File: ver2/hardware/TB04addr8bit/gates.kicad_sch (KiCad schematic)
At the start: 16 parts, among them U1501 74AHC04, U1502 74AHC04, U1503 74LS08, U1504 74HC00, U1505 74LS00, U1506 74LS32, U1507 74LS08, U1508 74HC00

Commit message: ver2: 掃除とタイミング是正(ROMのEXEゲート・フラグクロックをFCH1へ)
- 消費先ゼロだったU1302(RAM_SEL/STACK_SEL/IN_SEL/P6)を削除し空きゲート入力をGNDへ
- /OE_ROMの条件を生の~WRから~WR_EXE(=!(WR&EXE))へ変更
  書込命令の次のフェッチでROMが閉じる問題を解消
- フラグDFFのクロックゲートをEXEからFCH1へ(CLK_C=FCH1&C_WE)
  INのZが間に合わない件と、Cin=C_prevの帰還でADD/SUBの結果が壊れる件を解消
- いずれもネットリストで接続変化を照合済み。ERCはエラー98(全てwire_dangling)・警告0

Co-Authored-By: Claude Opus 5 <noreply@anthropic.com>
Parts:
- removed unit 4 of U1502
- added unit 4 of U1501
- renumbered U1502 to U1501, U1501 to U1502
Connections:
- net P4 is gone; now on net GND: U1501.3
- net EXE: no longer U1503.1, U1503.4
- net FCH1: now also U1503.1, U1503.4
- net WR_EXE: now also U1501.9
- net ~{WR}: no longer U1504.13
- net ~{P4}: no longer names the net of U1501.4
- new net ~{WR_EXE}: U1501.8, U1504.13
- no-connect marks 5 -> 6
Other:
- moved on the sheet: U1501B, U1501E, U1501F, U1502D, U1506D

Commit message: ver2: Yドライバ/PCドライバを1チップ1機能に整理
- ram: 74HC244×2を組み替え。U1102=Yドライバ専用(YD0-3→MD0-3、
  bank2はGND→MD4-7で上位0埋め、OE2本とも~YEN_Y)、U1103=PCドライバ
  専用(PC_Q0-7→MD0-7、OE2本とも~YEN_PC)。接続の集合は変更前と完全
  一致で機能等価。PCの8bitが1チップに揃いビット間スキューが揃う
- inPut: U1001のbank2イネーブル(pin19)をVDDから~OE_iAddrへ。
  出力2Y0-3はno_connectのままなので効果は未発現
- addrMUX/sp: 未使用出力のスタブ位置調整のみ(接続変更なし)

Co-Authored-By: Claude Opus 5 <noreply@anthropic.com>
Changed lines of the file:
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@@
 	)
 	(global_label "WR"
-		(shape input)
+		(shape output)
 		(at 55.88 35.56 0)
 		(fields_autoplaced yes)

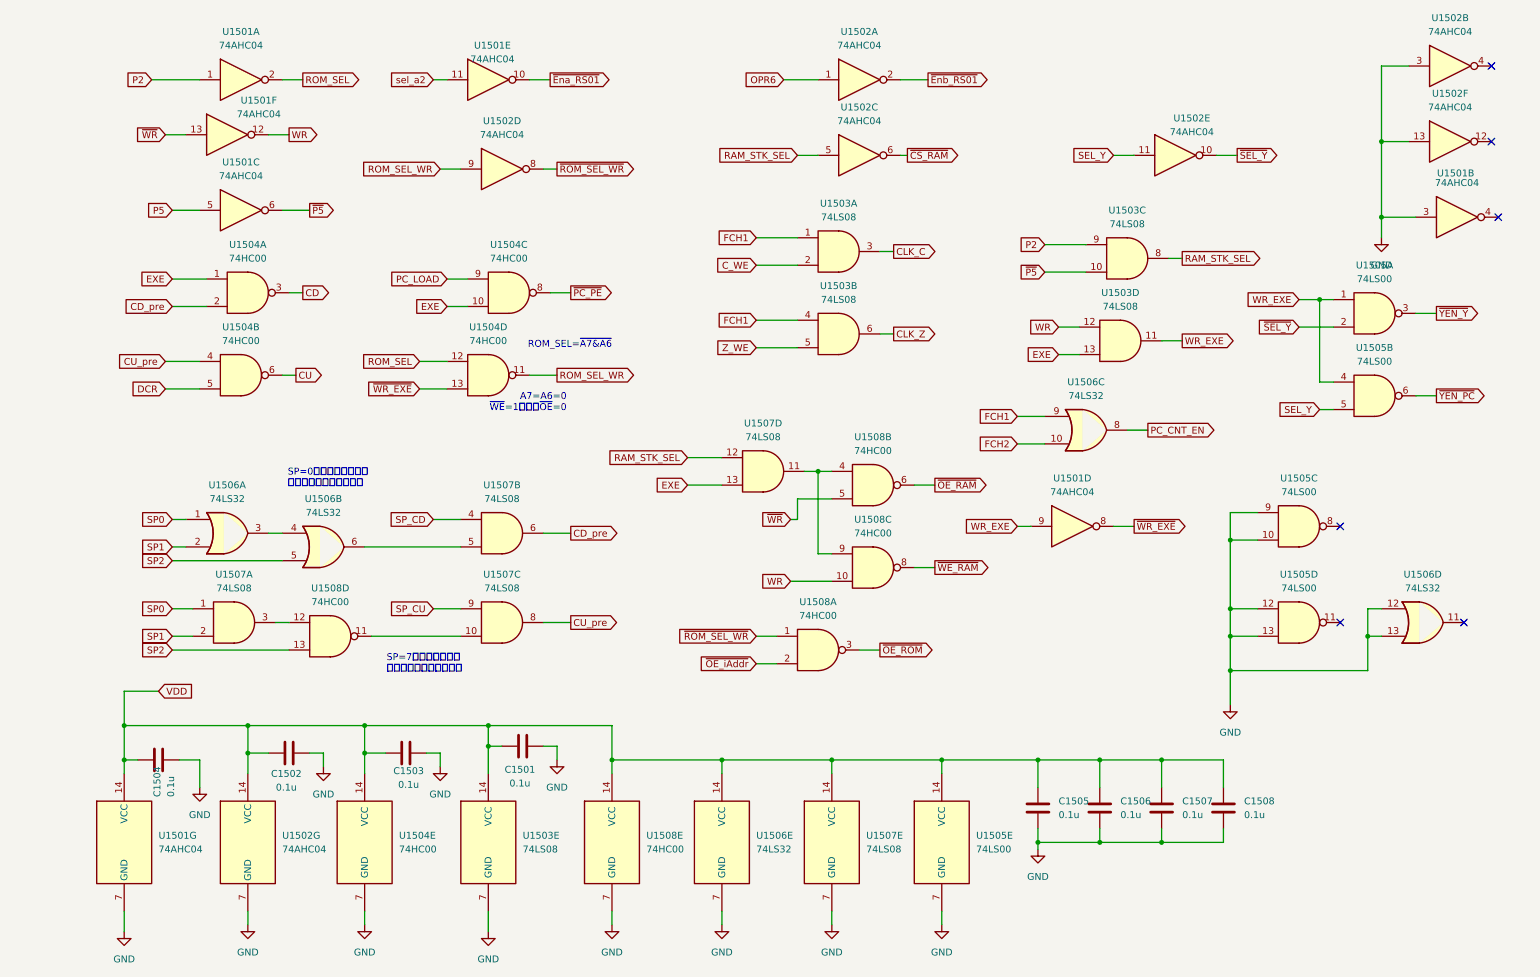
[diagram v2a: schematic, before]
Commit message: ver2: CALLの書込タイミングを是正(RAM書込パルスをCLK_CPUでゲート)
~WE_RAM = !(RAM_STK_SEL & EXE & WR & CLK_CPU) に変更し、
EXE前半のCLK立下りで書込を確定させる。CALLが戻り番地でなく
分岐先をスタックに書く問題を解消。gatesシートの空きゲート
(U1502インバータ・U1505 NAND g3)を使い追加ICは0個。

Co-Authored-By: Claude Opus 5 <noreply@anthropic.com>
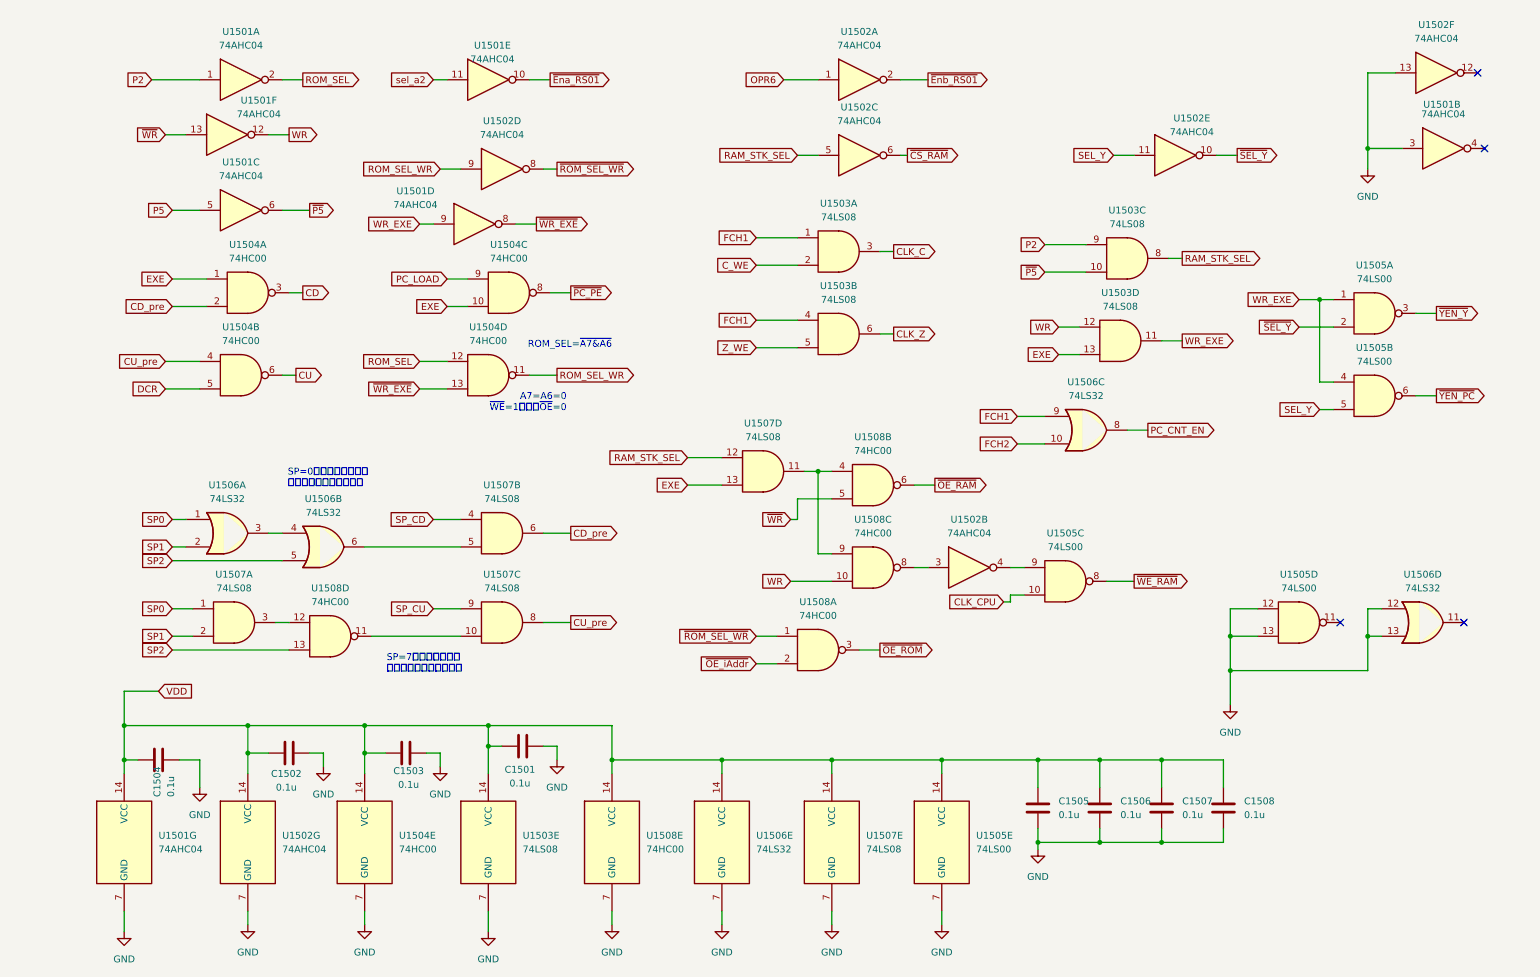
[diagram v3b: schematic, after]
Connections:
- net GND: no longer U1502.3, U1505.10, U1505.9
- net ~{WE_RAM}: now also U1505.8; no longer U1508.8
- net at U1502.4: now also U1505.9
- new net: U1502.3, U1508.8
- new net CLK_CPU: U1505.10
- no-connect marks 6 -> 4
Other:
- moved on the sheet: U1501B, U1501D, U1502B, U1502F, U1505C

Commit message: ver2: I/Oを4ch化しアドレスバスの浮きを解消(OUTは377化・RAMのCSをEXEゲート)
- I/Oアドレス源244・port位置MUX157・portデコード139を追加し、IN244×4/OUT×4に拡張。
  IN/OUT実行中も 0xF8|port / 0xFC|port をアドレスバスへ出すことで、全相・全命令で
  アドレスバスが必ず1つに駆動される状態にした(OUTのRAM誤書込・INのMD衝突を構造的に解消)。
- OUTポートを74HC273→74HC377へ。~E=139出力・CP=~CLK_CPUとし、クロックゲートなしで
  EXE中間の1回だけ取り込む(取り込み余裕が15ns→半相)。
- ~CS_RAM を !(RAM_STK_SEL & EXE) に変更(CS_RAMノード新設)。EXE末に出る第2の書込パルスを
  約38nsに短縮しtWP未満に収めた。フェッチ3相でRAMが非選択になる副次効果あり。
- OUTコネクタのピン配列を7segIF J1に合わせて入れ替え(D3出力がVDDへ短絡する組合せを回避)。
- パスコンが無かった2シート(outPort・PC_aluMux)に追加。RS.kicad_sch を RS00.kicad_sch へ改名。

Co-Authored-By: Claude Opus 5 <noreply@anthropic.com>
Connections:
- net EXE: now also U1505.13
- net GND: no longer U1505.12, U1505.13
- net RAM_STK_SEL: no longer U1502.5
- net CS_RAM: now reaches U1507.11, U1508.4, U1508.9
- net CS_RAM: now also U1502.5
- net ~{OE_ioAddr}: now reaches U1505.11
- new net SEL_M1: U1505.12
- no-connect marks 4 -> 3
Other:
- moved on the sheet: U1505D, U1506D

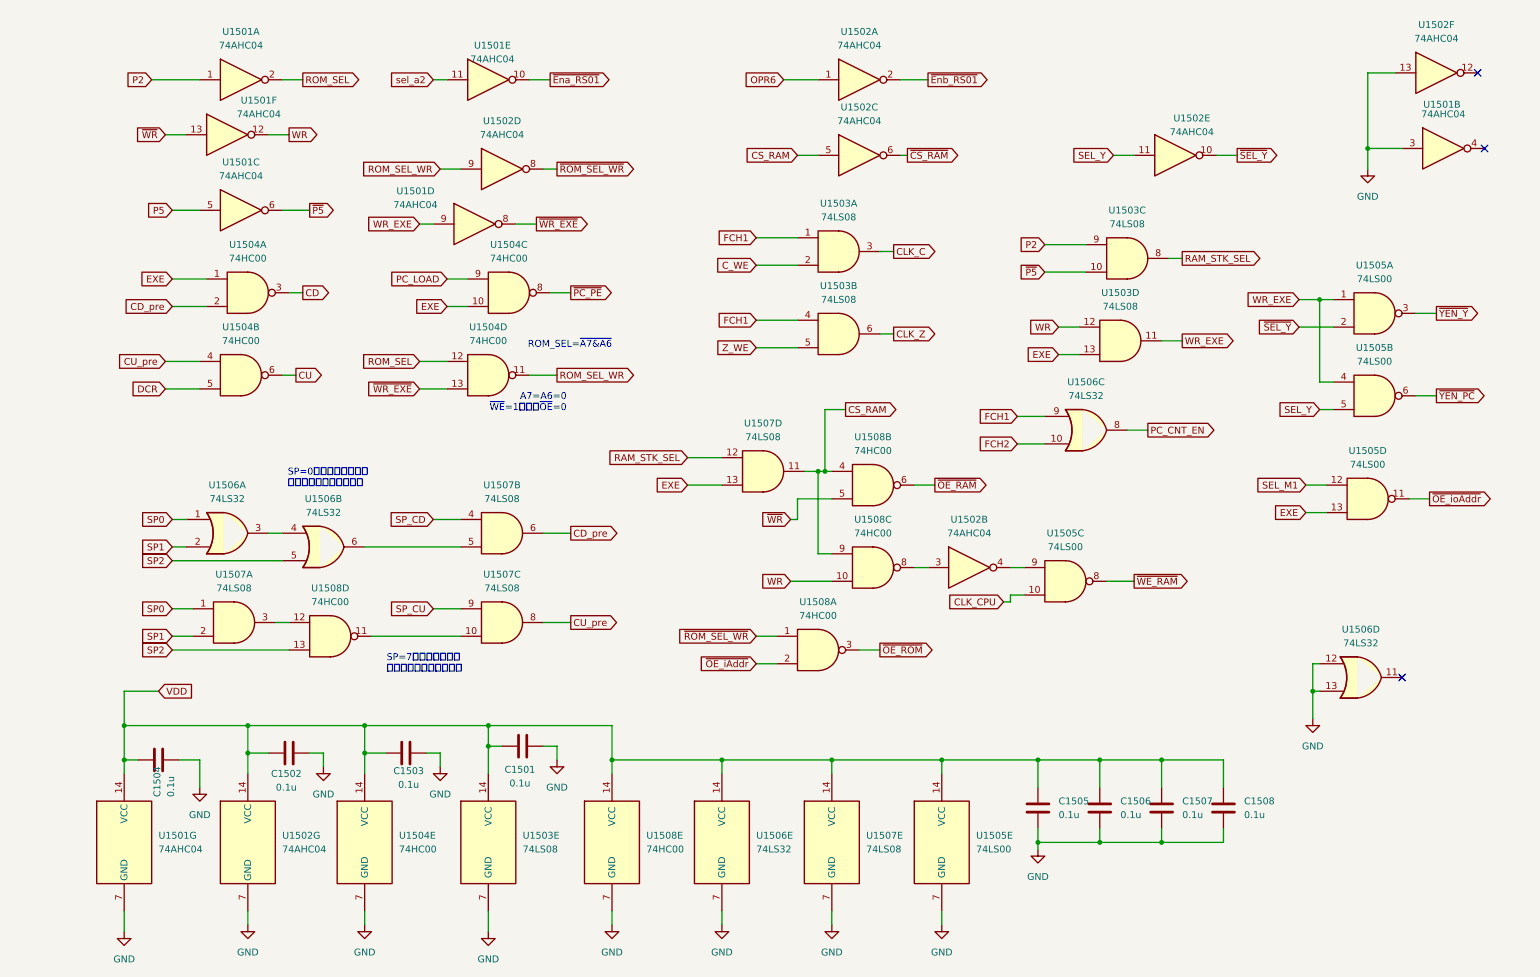
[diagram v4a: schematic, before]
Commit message: ver2: SPアップカウントのヒゲを除去(CUをCLK_CPUでマスク)
CU=!(CU_pre & DCR)のCU_preがDCR自身でクロックされる制御ラッチU701から
来ているため、POP/RETの次の命令のDCR立上りで幅22-46nsのヒゲが出てSPが
余分に+1されていた(3段以上のネストで戻り番地がずれる)。

U1506の空きORゲートでCU=!(CU_pre & DCR & ~CLK_CPU)とし、DCR開始時は
CLK_CPUがHなのでヒゲをマスクする。カウント用の立上りは従来どおり
DCR→EXEの境目に出るのでプリインクリメントの意味は変わらない。

Co-Authored-By: Claude Opus 5 <noreply@anthropic.com>
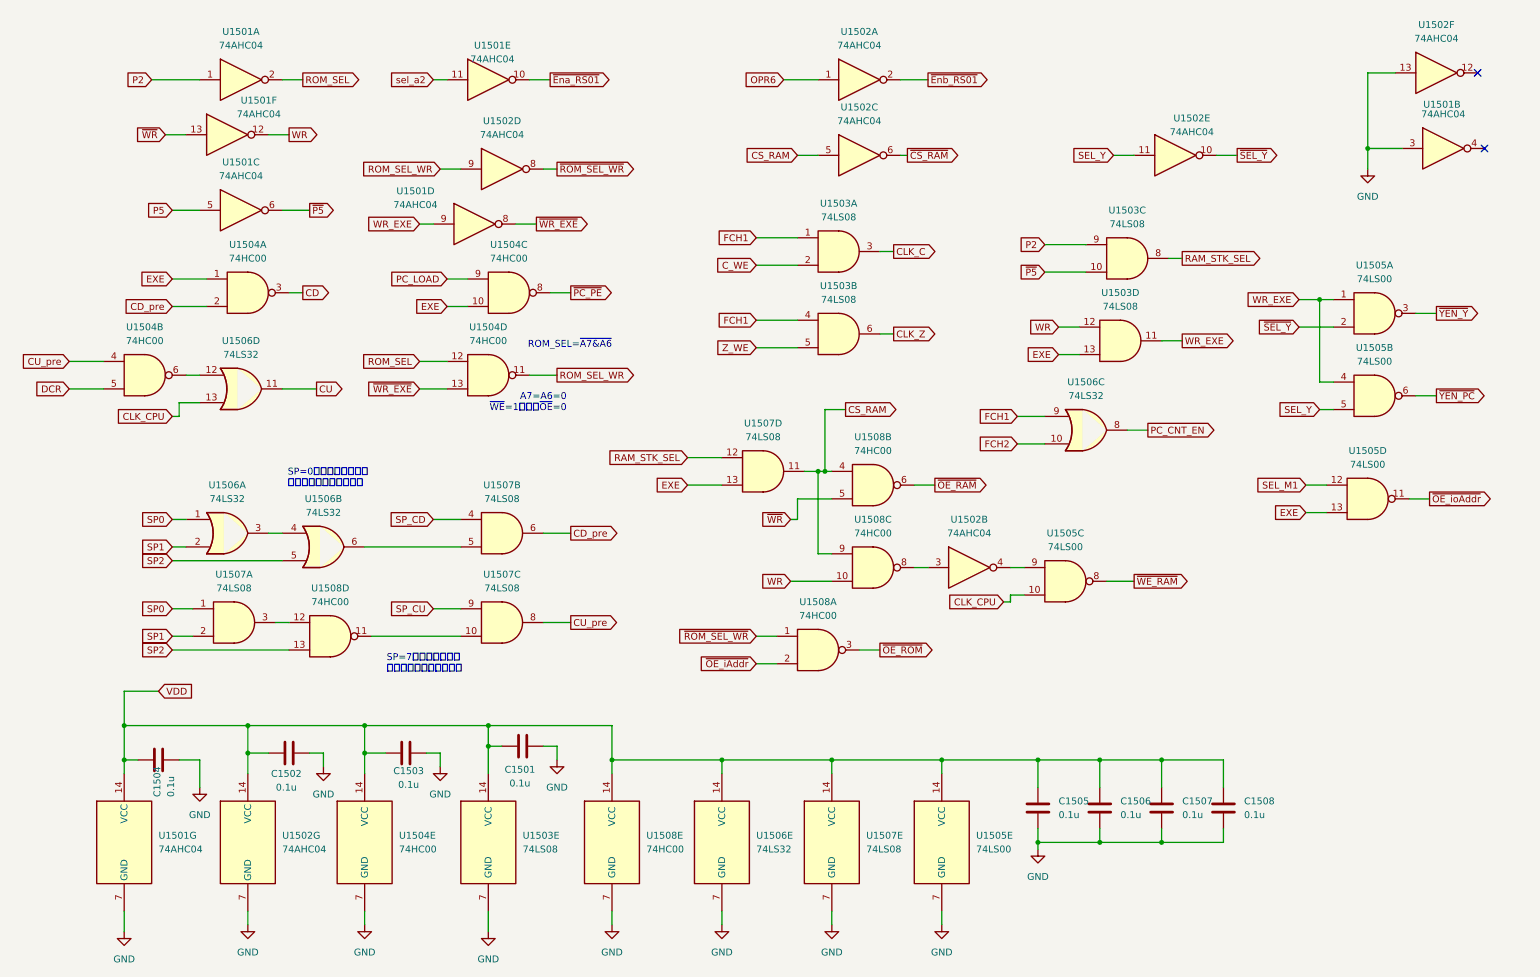
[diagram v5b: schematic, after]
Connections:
- net CLK_CPU: now also U1506.13
- net CU: now also U1506.11; no longer U1504.6
- net GND: no longer U1506.12, U1506.13
- new net: U1504.6, U1506.12
- no-connect marks 3 -> 2
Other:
- moved on the sheet: U1504B, U1506D
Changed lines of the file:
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@@
 	)
 	(junction
-		(at 245.11 138.43)
-		(diameter 0)
-		(color 0 0 0 0)
-	)
-	(junction
 		(at 154.94 97.79)
 		(diameter 0)
@@
 	)
 	(no_connect
-		(at 261.62 135.89)
-	)
-	(no_connect
 		(at 276.86 38.1)
 	)
@@
 	(wire
 		(pts
-			(xy 245.11 138.43) (xy 246.38 138.43)
-		)
-		(stroke
-			(width 0)
-			(type default)
-		)
-	)
-	(wire
-		(pts
 			(xy 217.17 151.13) (xy 217.17 156.21)
 		)
@@
 	(wire
 		(pts
+			(xy 35.56 87.63) (xy 35.56 85.09)
+		)
+		(stroke
+			(width 0)
+			(type default)
+		)
+	)
+	(wire
+		(pts
 			(xy 255.27 38.1) (xy 261.62 38.1)
 		)
@@
 	(wire
 		(pts
+			(xy 34.29 87.63) (xy 35.56 87.63)
+		)
+		(stroke
+			(width 0)
+			(type default)
+		)
+	)
+	(wire
+		(pts
 			(xy 48.26 149.86) (xy 52.07 149.86)
 		)
@@
 	(wire
 		(pts
-			(xy 33.02 77.47) (xy 39.37 77.47)
+			(xy 15.24 77.47) (xy 21.59 77.47)
 		)
 		(stroke
@@
 	(wire
 		(pts
-			(xy 33.02 82.55) (xy 39.37 82.55)
+			(xy 15.24 82.55) (xy 21.59 82.55)
 		)
 		(stroke
@@
 	(wire
 		(pts
-			(xy 245.11 133.35) (xy 245.11 138.43)
-		)
-		(stroke
-			(width 0)
-			(type default)
-		)
-	)
-	(wire
-		(pts
 			(xy 195.58 60.96) (xy 203.2 60.96)
 		)
@@
 	(wire
 		(pts
-			(xy 54.61 25.4) (xy 58.42 25.4)
+			(xy 54.61 82.55) (xy 60.96 82.55)
 		)
 		(stroke
@@
 	(wire
 		(pts
-			(xy 153.67 97.79) (xy 154.94 97.79)
+			(xy 54.61 25.4) (xy 58.42 25.4)
 		)
 		(stroke
@@
 	(wire
 		(pts
-			(xy 30.48 25.4) (xy 39.37 25.4)
+			(xy 153.67 97.79) (xy 154.94 97.79)
 		)
 		(stroke
@@
 	(wire
 		(pts
-			(xy 135.89 151.13) (xy 156.21 151.13)
+			(xy 30.48 25.4) (xy 39.37 25.4)
 		)
 		(stroke
@@
 	(wire
 		(pts
-			(xy 135.89 151.13) (xy 135.89 153.67)
+			(xy 135.89 151.13) (xy 156.21 151.13)
 		)
 		(stroke
@@
 	(wire
 		(pts
-			(xy 246.38 133.35) (xy 245.11 133.35)
+			(xy 135.89 151.13) (xy 135.89 153.67)
 		)
 		(stroke
@@
 	(wire
 		(pts
-			(xy 54.61 80.01) (xy 57.15 80.01)
+			(xy 36.83 80.01) (xy 39.37 80.01)
 		)
 		(stroke
@@
 	(wire
 		(pts
-			(xy 245.11 138.43) (xy 245.11 143.51)
-		)
-		(stroke
-			(width 0)
-			(type default)
-		)
-	)
-	(wire
-		(pts
 			(xy 264.16 83.82) (xy 267.97 83.82)
 		)
@@
 		)
 	)
+	(wire
+		(pts
+			(xy 35.56 85.09) (xy 39.37 85.09)
+		)
+		(stroke
+			(width 0)
+			(type default)
+		)
+	)
 	(global_label "FCH1"
 		(shape input)
@@
 		)
 	)
+	(global_label "CLK_CPU"
+		(shape input)
+		(at 34.29 87.63 180)
+		(fields_autoplaced yes)
+		(effects
+			(font
+				(size 1.27 1.27)
+			)
+			(justify right)
+		)
+		(property "Intersheetrefs" "${INTERSHEET_REFS}"
+			(at 22.8986 87.63 0)
+			(show_name no)
+			(do_not_autoplace no)
+			(effects
+				(font
+					(size 1.27 1.27)
+				)
+				(justify right)
+			)
+		)
+	)
 	(global_label "P2"
 		(shape input)
@@
 	(global_label "DCR"
 		(shape input)
-		(at 33.02 82.55 180)
+		(at 15.24 82.55 180)
 		(fields_autoplaced yes)
 		(effects
@@
 		)
 		(property "Intersheetrefs" "${INTERSHEET_REFS}"
-			(at 23.5034 82.55 0)
+			(at 5.7234 82.55 0)
 			(show_name no)
 			(do_not_autoplace no)
@@
 	(global_label "CU"
 		(shape output)
-		(at 57.15 80.01 0)
+		(at 60.96 82.55 0)
 		(fields_autoplaced yes)
 		(effects
@@
 		)
 		(property "Intersheetrefs" "${INTERSHEET_REFS}"
-			(at 62.7357 80.01 0)
+			(at 66.5457 82.55 0)
 			(show_name no)
 			(do_not_autoplace no)
@@
 	(global_label "CU_pre"
 		(shape input)
-		(at 33.02 77.47 180)
+		(at 15.24 77.47 180)
 		(fields_autoplaced yes)
 		(effects
@@
 		)
 		(property "Intersheetrefs" "${INTERSHEET_REFS}"
-			(at 23.4429 77.47 0)
+			(at 5.6629 77.47 0)
 			(show_name no)
 			(do_not_autoplace no)
@@
 	)
 	(symbol
-		(lib_id "power:GND")
-		(at 245.11 143.51 0)
-		(unit 1)
-		(body_style 1)
-		(exclude_from_sim no)
-		(in_bom yes)
-		(on_board yes)
-		(in_pos_files yes)
-		(dnp no)
-		(fields_autoplaced yes)
-		(property "Reference" "#PWR01502"
-			(at 245.11 149.86 0)
-			(hide yes)
-			(show_name no)
-			(do_not_autoplace no)
-			(effects
-				(font
-					(size 1.27 1.27)
-				)
-			)
-		)
-		(property "Value" "GND"
-			(at 245.11 148.59 0)
-			(show_name no)
-			(do_not_autoplace no)
-			(effects
-				(font
-					(size 1.27 1.27)
-				)
-			)
-		)
-		(property "Footprint" ""
-			(at 245.11 143.51 0)
-			(hide yes)
-			(show_name no)
-			(do_not_autoplace no)
-			(effects
-				(font
-					(size 1.27 1.27)
-				)
-			)
-		)
-		(property "Datasheet" ""
-			(at 245.11 143.51 0)
-			(hide yes)
-			(show_name no)
-			(do_not_autoplace no)
-			(effects
-				(font
-					(size 1.27 1.27)
-				)
-			)
-		)
-		(property "Description" "Power symbol creates a global label with name \"GND\" , ground"
-			(at 245.11 143.51 0)
-			(hide yes)
-			(show_name no)
-			(do_not_autoplace no)
-			(effects
-				(font
-					(size 1.27 1.27)
-				)
-			)
-		)
-		(pin "1"
-		)
-		(instances
-			(project "TB04addr8bit"
-				(path "/d176c79b-dced-4d01-bcec-7dfd676fcfc2/5f2ddf07-9846-470a-9333-ad8d658dfcaf"
-					(reference "#PWR01502")
-					(unit 1)
-				)
-			)
-		)
-	)
-	(symbol
 		(lib_id "74xx:74LS08")
 		(at 95.25 125.73 0)
@@
 	(symbol
 		(lib_id "74xx:74LS32")
-		(at 254 135.89 0)
+		(at 46.99 82.55 0)
 		(unit 4)
 		(body_style 1)
@@
 		(fields_autoplaced yes)
 		(property "Reference" "U1506"
-			(at 254 127 0)
+			(at 46.99 73.66 0)
 			(show_name no)
 			(do_not_autoplace no)
@@
 		)
 		(property "Value" "74LS32"
-			(at 254 129.54 0)
+			(at 46.99 76.2 0)
 			(show_name no)
 			(do_not_autoplace no)
@@
 		)
 		(property "Footprint" ""
-			(at 254 135.89 0)
+			(at 46.99 82.55 0)
 			(hide yes)
 			(show_name no)
@@
 		)
 		(property "Datasheet" "http://www.ti.com/lit/gpn/sn74LS32"
-			(at 254 135.89 0)
+			(at 46.99 82.55 0)
 			(hide yes)
 			(show_name no)
@@
 		)
 		(property "Description" "Quad 2-input OR"
-			(at 254 135.89 0)
+			(at 46.99 82.55 0)
 			(hide yes)
 			(show_name no)
@@
 	(symbol
 		(lib_id "74xx:74HC00")
-		(at 46.99 80.01 0)
+		(at 29.21 80.01 0)
 		(unit 2)
 		(body_style 1)
@@
 		(fields_autoplaced yes)
 		(property "Reference" "U1504"
-			(at 46.9817 71.12 0)
+			(at 29.2017 71.12 0)
 			(show_name no)
 			(do_not_autoplace no)
@@
 		)
 		(property "Value" "74HC00"
-			(at 46.9817 73.66 0)
+			(at 29.2017 73.66 0)
 			(show_name no)
 			(do_not_autoplace no)
@@
 		)
 		(property "Footprint" ""
-			(at 46.99 80.01 0)
+			(at 29.21 80.01 0)
 			(hide yes)
 			(show_name no)
@@
 		)
 		(property "Datasheet" "http://www.ti.com/lit/gpn/sn74hc00"
-			(at 46.99 80.01 0)
+			(at 29.21 80.01 0)
 			(hide yes)
 			(show_name no)
@@
 		)
 		(property "Description" "quad 2-input NAND gate"
-			(at 46.99 80.01 0)
+			(at 29.21 80.01 0)
 			(hide yes)
 			(show_name no)
